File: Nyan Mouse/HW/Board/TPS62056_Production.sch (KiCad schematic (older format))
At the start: 7 parts

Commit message: A lot of kicad.... A LOT.
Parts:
- removed C? (x2): 22uF, symbol CP1
- removed L?: 10uH, symbol INDUCTOR_SMALL
- removed R?: 510K, symbol R
- removed R?: 110K, symbol R
- removed R?: 510k, symbol R
- removed U?: TPS6205X, symbol TPS6205X
- added C? (x2): 22uF, symbol CP1
- added L?: 10uH, symbol INDUCTOR_SMALL
- added R?: 510K, symbol R
- added R?: 110K, symbol R
- added R?: 510k, symbol R
- added U?: TPS6205X, symbol TPS6205X
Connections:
- net 3.3VOUT: now also C?.1, L?.2, R?.1, U?.5 (FB)
- net GND: now also C?.2, C?.2, R?.2, U?.10 (PGND), U?.3 (GND), U?.4 (PG), U?.7 (SYNC)
- net VIN: now also C?.1, R?.1, U?.1 (VIN), U?.8 (EN)
- new net: R?.2, U?.2 (LBO)
- new net: R?.1, R?.2, U?.6 (LBI)
- new net: L?.1, U?.9 (SW)
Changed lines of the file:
@@
 LIBS:3v3custom
 LIBS:altera_ep4ce15e22c
+LIBS:mic94345-4ycs
+LIBS:lp3987
+LIBS:s25fl064p
 LIBS:Nyan Mouse-cache
+LIBS:TPS62056_Production-cache
 EELAYER 24 0
 EELAYER END
 $Descr USLetter 11000 8500
 encoding utf-8
-Sheet 2 6
+Sheet 4 5
 Title "Nyan Mouse"
-Date "20 Apr 2014"
+Date "22 Apr 2014"
 Rev "Alpha"
 Comp "IEEE UCR"
@@
 $Comp
 L TPS6205X U?
-U 1 1 535478BD
+U 1 1 535727C9
 P 3300 2500
-AR Path="/53547798/535478BD" Ref="U?"  Part="1"
-AR Path="/535488D9/535478BD" Ref="U?"  Part="1"
+AR Path="/535488D9/535727C9" Ref="U?"  Part="1"
+AR Path="/53573052/535727C9" Ref="U?"  Part="1"
 F 0 "U?" H 2850 2750 60  0000 C CNN
 F 1 "TPS6205X" H 3300 2200 60  0000 C CNN
@@
 $Comp
 L CP1 C?
-U 1 1 5354790A
+U 1 1 535727CA
 P 1100 2700
-AR Path="/53547798/5354790A" Ref="C?"  Part="1"
-AR Path="/535488D9/5354790A" Ref="C?"  Part="1"
+AR Path="/535488D9/535727CA" Ref="C?"  Part="1"
+AR Path="/53573052/535727CA" Ref="C?"  Part="1"
 F 0 "C?" H 1150 2800 50  0000 L CNN
 F 1 "22uF" H 1150 2600 50  0000 L CNN
@@
 $Comp
 L R R?
-U 1 1 5354793A
+U 1 1 535727CB
 P 1550 2750
-AR Path="/53547798/5354793A" Ref="R?"  Part="1"
-AR Path="/535488D9/5354793A" Ref="R?"  Part="1"
+AR Path="/535488D9/535727CB" Ref="R?"  Part="1"
+AR Path="/53573052/535727CB" Ref="R?"  Part="1"
 F 0 "R?" V 1630 2750 40  0000 C CNN
 F 1 "510K" V 1557 2751 40  0000 C CNN
@@
 $Comp
 L R R?
-U 1 1 5354794E
+U 1 1 535727CC
 P 1550 3350
-AR Path="/53547798/5354794E" Ref="R?"  Part="1"
-AR Path="/535488D9/5354794E" Ref="R?"  Part="1"
+AR Path="/535488D9/535727CC" Ref="R?"  Part="1"
+AR Path="/53573052/535727CC" Ref="R?"  Part="1"
 F 0 "R?" V 1630 3350 40  0000 C CNN
 F 1 "110K" V 1557 3351 40  0000 C CNN
@@
 $Comp
 L R R?
-U 1 1 535479CB
+U 1 1 535727CD
 P 4850 2750
-AR Path="/53547798/535479CB" Ref="R?"  Part="1"
-AR Path="/535488D9/535479CB" Ref="R?"  Part="1"
+AR Path="/535488D9/535727CD" Ref="R?"  Part="1"
+AR Path="/53573052/535727CD" Ref="R?"  Part="1"
 F 0 "R?" V 4930 2750 40  0000 C CNN
 F 1 "510k" V 4857 2751 40  0000 C CNN
@@
 $Comp
 L INDUCTOR_SMALL L?
-U 1 1 53547A93
+U 1 1 535727CE
 P 4450 2500
-AR Path="/53547798/53547A93" Ref="L?"  Part="1"
-AR Path="/535488D9/53547A93" Ref="L?"  Part="1"
+AR Path="/535488D9/535727CE" Ref="L?"  Part="1"
+AR Path="/53573052/535727CE" Ref="L?"  Part="1"
 F 0 "L?" H 4450 2600 50  0000 C CNN
 F 1 "10uH" H 4450 2450 50  0000 C CNN
@@
 $Comp
 L CP1 C?
-U 1 1 53547BCD
+U 1 1 535727CF
 P 5100 2700
-AR Path="/53547798/53547BCD" Ref="C?"  Part="1"
-AR Path="/535488D9/53547BCD" Ref="C?"  Part="1"
+AR Path="/535488D9/535727CF" Ref="C?"  Part="1"
+AR Path="/53573052/535727CF" Ref="C?"  Part="1"
 F 0 "C?" H 5150 2800 50  0000 L CNN
 F 1 "22uF" H 5150 2600 50  0000 L CNN

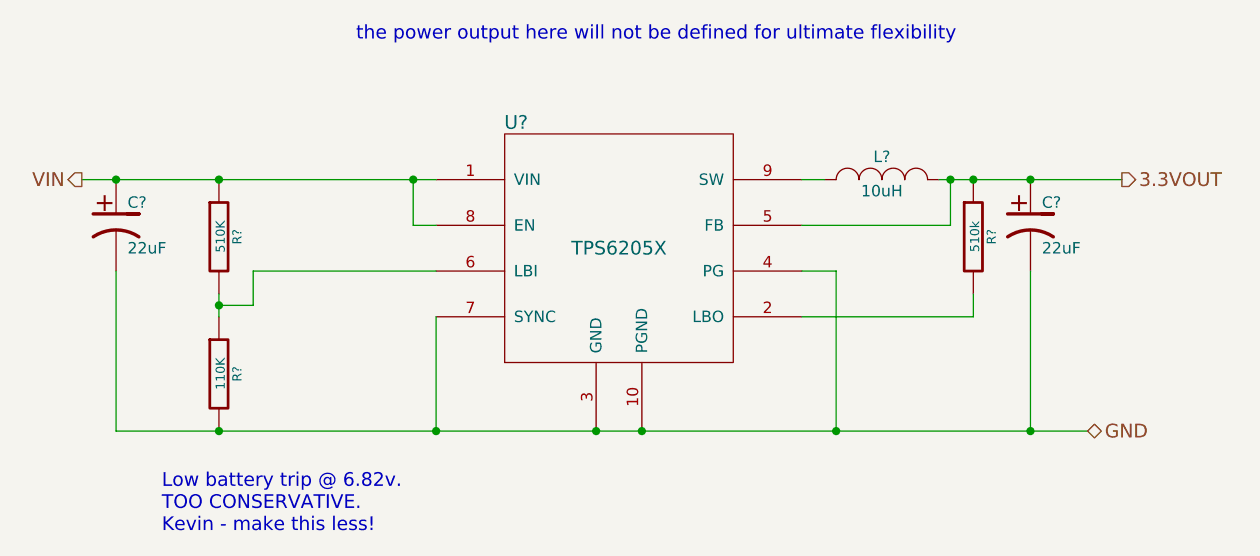
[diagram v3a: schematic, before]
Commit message: Changed DRV8837, Almost completed main board. ERC almost successful.
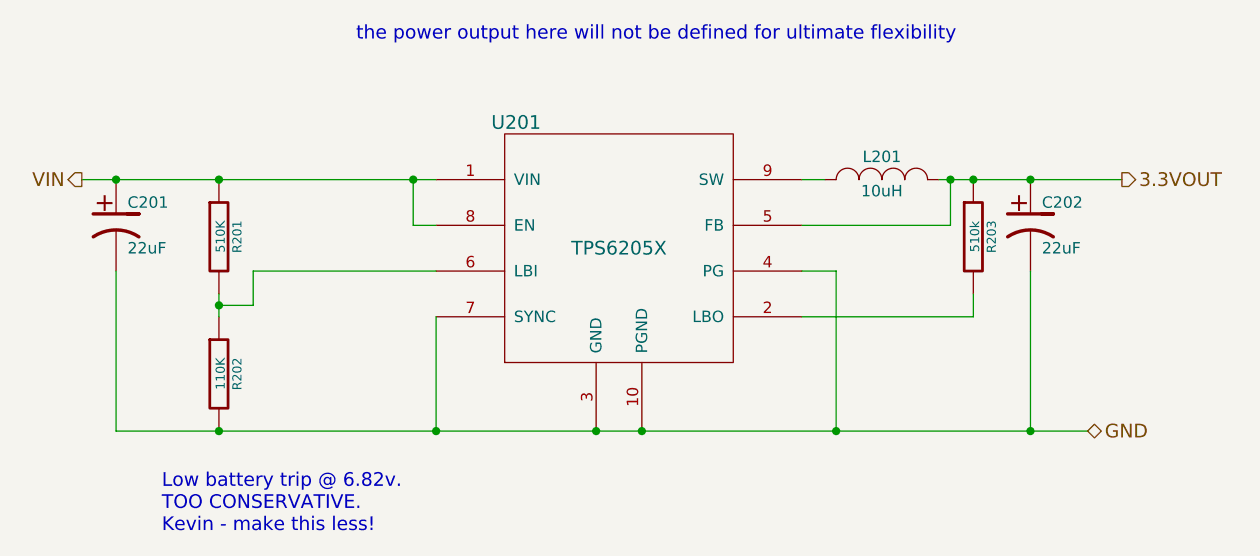
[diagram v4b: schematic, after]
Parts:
- gave numbers to parts that had none: 7
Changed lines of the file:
@@
 Sheet 4 5
 Title "Nyan Mouse"
-Date "22 Apr 2014"
+Date "23 Apr 2014"
 Rev "Alpha"
 Comp "IEEE UCR"
@@
 $EndDescr
 $Comp
-L TPS6205X U?
+L TPS6205X U201
 U 1 1 535727C9
 P 3300 2500
-AR Path="/535488D9/535727C9" Ref="U?"  Part="1"
-AR Path="/53573052/535727C9" Ref="U?"  Part="1"
-F 0 "U?" H 2850 2750 60  0000 C CNN
+AR Path="/535488D9/535727C9" Ref="U201"  Part="1"
+AR Path="/53573052/535727C9" Ref="U401"  Part="1"
+F 0 "U201" H 2850 2750 60  0000 C CNN
 F 1 "TPS6205X" H 3300 2200 60  0000 C CNN
 F 2 "" H 2500 2650 60  0000 C CNN
@@
 $EndComp
 $Comp
-L CP1 C?
+L CP1 C201
 U 1 1 535727CA
 P 1100 2700
-AR Path="/535488D9/535727CA" Ref="C?"  Part="1"
-AR Path="/53573052/535727CA" Ref="C?"  Part="1"
-F 0 "C?" H 1150 2800 50  0000 L CNN
+AR Path="/535488D9/535727CA" Ref="C201"  Part="1"
+AR Path="/53573052/535727CA" Ref="C401"  Part="1"
+F 0 "C201" H 1150 2800 50  0000 L CNN
 F 1 "22uF" H 1150 2600 50  0000 L CNN
 F 2 "" H 1100 2700 60  0000 C CNN
@@
 $EndComp
 $Comp
-L R R?
+L R R201
 U 1 1 535727CB
 P 1550 2750
-AR Path="/535488D9/535727CB" Ref="R?"  Part="1"
-AR Path="/53573052/535727CB" Ref="R?"  Part="1"
-F 0 "R?" V 1630 2750 40  0000 C CNN
+AR Path="/535488D9/535727CB" Ref="R201"  Part="1"
+AR Path="/53573052/535727CB" Ref="R401"  Part="1"
+F 0 "R201" V 1630 2750 40  0000 C CNN
 F 1 "510K" V 1557 2751 40  0000 C CNN
 F 2 "" V 1480 2750 30  0000 C CNN
@@
 $EndComp
 $Comp
-L R R?
+L R R202
 U 1 1 535727CC
 P 1550 3350
-AR Path="/535488D9/535727CC" Ref="R?"  Part="1"
-AR Path="/53573052/535727CC" Ref="R?"  Part="1"
-F 0 "R?" V 1630 3350 40  0000 C CNN
+AR Path="/535488D9/535727CC" Ref="R202"  Part="1"
+AR Path="/53573052/535727CC" Ref="R402"  Part="1"
+F 0 "R202" V 1630 3350 40  0000 C CNN
 F 1 "110K" V 1557 3351 40  0000 C CNN
 F 2 "" V 1480 3350 30  0000 C CNN
@@
 Connection ~ 3400 3600
 $Comp
-L R R?
+L R R203
 U 1 1 535727CD
 P 4850 2750
-AR Path="/535488D9/535727CD" Ref="R?"  Part="1"
-AR Path="/53573052/535727CD" Ref="R?"  Part="1"
-F 0 "R?" V 4930 2750 40  0000 C CNN
+AR Path="/535488D9/535727CD" Ref="R203"  Part="1"
+AR Path="/53573052/535727CD" Ref="R403"  Part="1"
+F 0 "R203" V 4930 2750 40  0000 C CNN
 F 1 "510k" V 4857 2751 40  0000 C CNN
 F 2 "" V 4780 2750 30  0000 C CNN
@@
 	1100 3600 1100 2900
 $Comp
-L INDUCTOR_SMALL L?
+L INDUCTOR_SMALL L201
 U 1 1 535727CE
 P 4450 2500
-AR Path="/535488D9/535727CE" Ref="L?"  Part="1"
-AR Path="/53573052/535727CE" Ref="L?"  Part="1"
-F 0 "L?" H 4450 2600 50  0000 C CNN
+AR Path="/535488D9/535727CE" Ref="L201"  Part="1"
+AR Path="/53573052/535727CE" Ref="L401"  Part="1"
+F 0 "L201" H 4450 2600 50  0000 C CNN
 F 1 "10uH" H 4450 2450 50  0000 C CNN
 F 2 "" H 4450 2500 60  0000 C CNN
@@
 	5100 2900 5100 3600
 $Comp
-L CP1 C?
+L CP1 C202
 U 1 1 535727CF
 P 5100 2700
-AR Path="/535488D9/535727CF" Ref="C?"  Part="1"
-AR Path="/53573052/535727CF" Ref="C?"  Part="1"
-F 0 "C?" H 5150 2800 50  0000 L CNN
+AR Path="/535488D9/535727CF" Ref="C202"  Part="1"
+AR Path="/53573052/535727CF" Ref="C402"  Part="1"
+F 0 "C202" H 5150 2800 50  0000 L CNN
 F 1 "22uF" H 5150 2600 50  0000 L CNN
 F 2 "" H 5100 2700 60  0000 C CNN
